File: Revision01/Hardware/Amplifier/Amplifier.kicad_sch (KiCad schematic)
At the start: 12 parts, among them U1 INA333AIDGKR, U2 TLV9061SQDBVRQ1

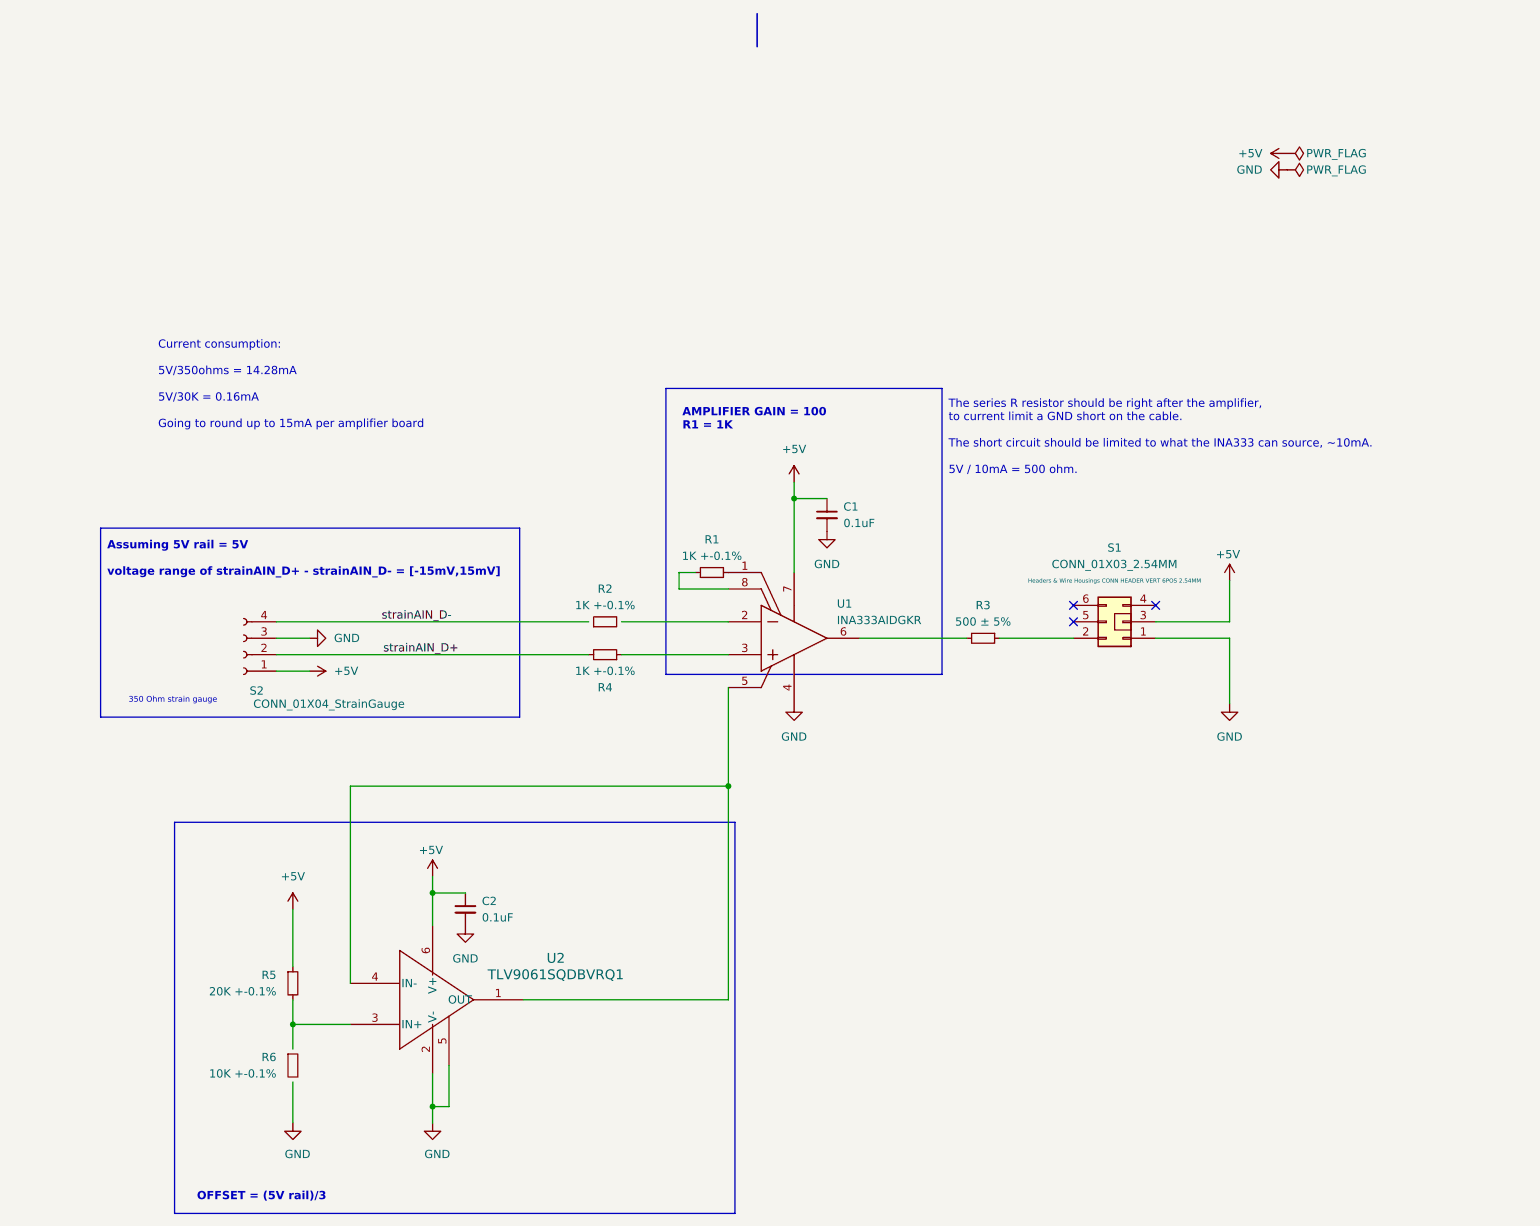
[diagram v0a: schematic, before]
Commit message: . Reverted Hardware/ changes to last known good commit f7a44a23fed9aca3ce7036a9f440c4d810a77518
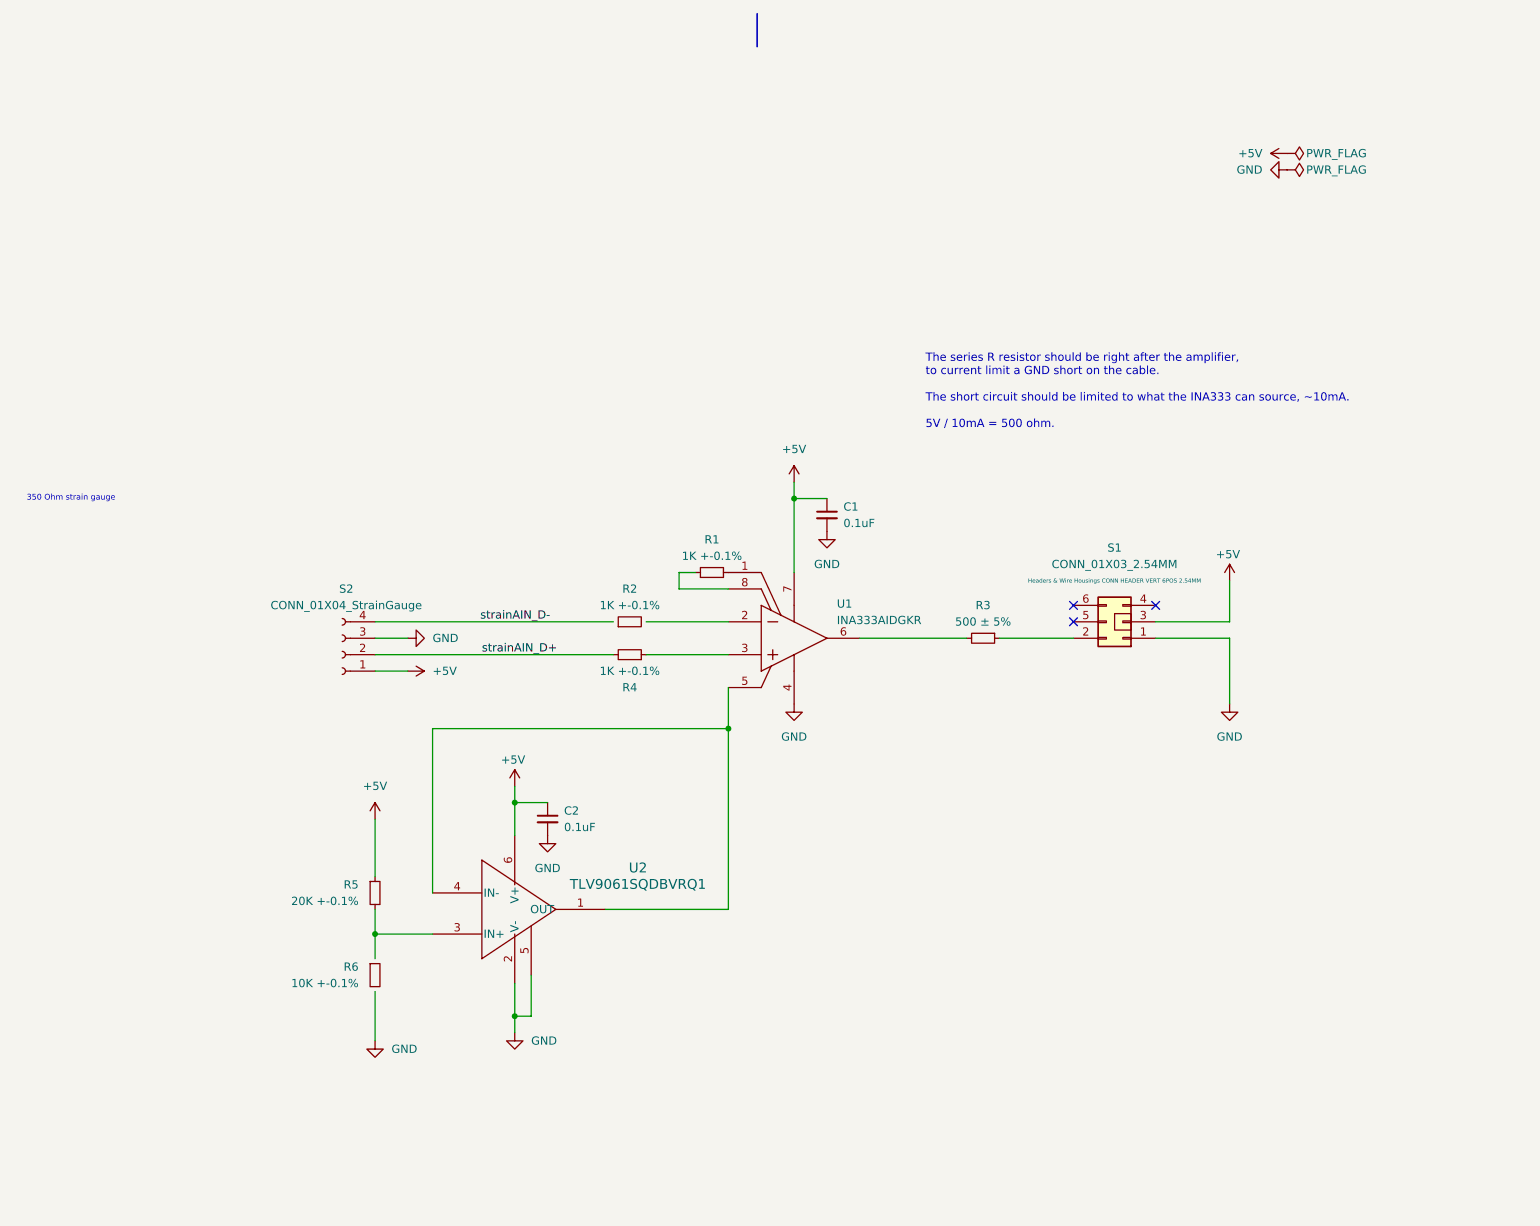
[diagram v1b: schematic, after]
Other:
- note removed: "AMPLIFIER GAIN = 100 R1 = 1K"
- note removed: "Assuming 5V rail = 5V voltage range of strainAIN_D+ - strainAIN_D- = [-15mV,15mV]"
- note removed: "Current consumption: 5V/350ohms = 14.28mA 5V/30K = 0.16mA Going to round up to 15mA per amplifier board"
- note removed: "OFFSET = (5V rail)/3"
- moved on the sheet: C2, R2, R4, R5, R6, S2, U2

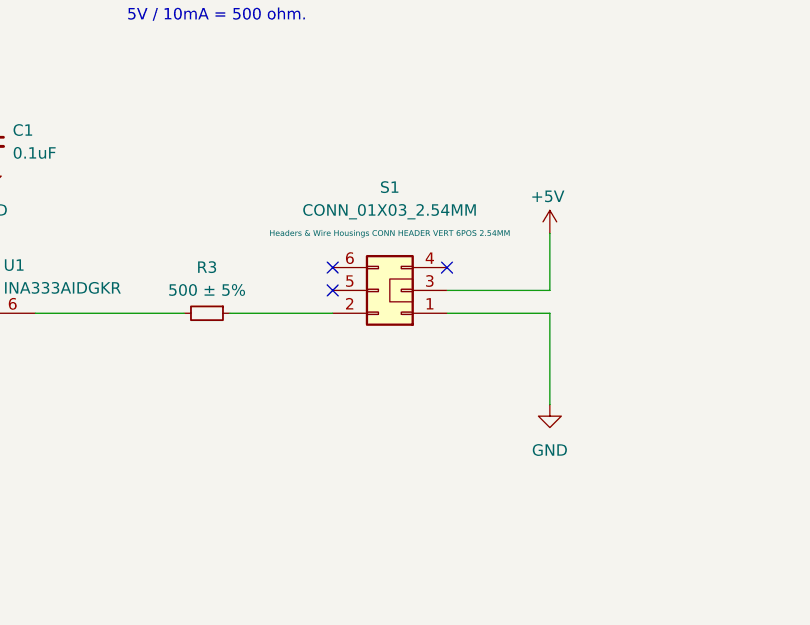
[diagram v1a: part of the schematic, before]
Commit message: . Hub & Amp: Changed wiring standard to GND SIG GND GND PWR GND . Hub: Added GND plane to 3.3V . Hub: Moved 1M pulldown resistor . Hub & Amp: Adjusted thermal relief tolerances . Hub: Changed buck convertor layout so capacitors are inline with feedback pin . Hub: Added stitching vias . Hub & Amp: Changed font sizes, changed silkscreen to be oriented one way
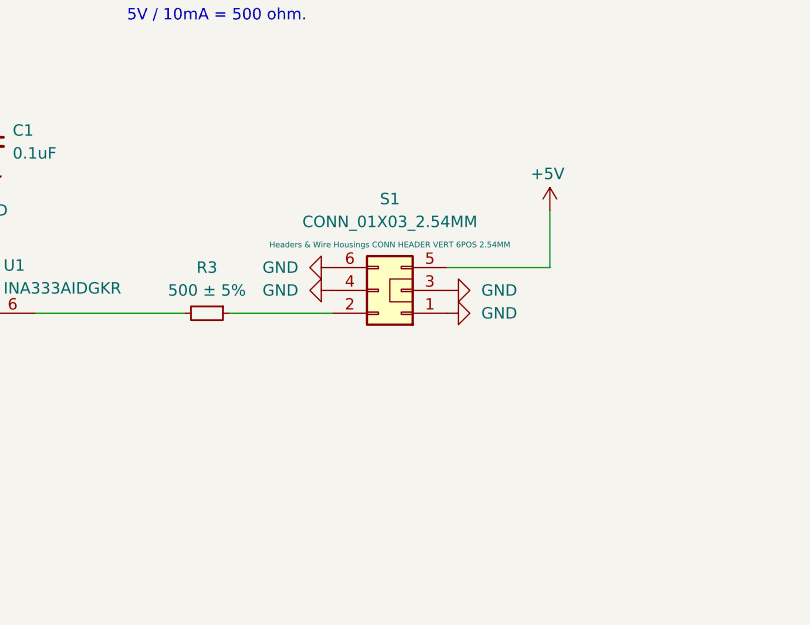
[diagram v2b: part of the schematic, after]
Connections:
- net +5V: now also S1.5 (Pin_5); no longer S1.3 (Pin_3)
- net GND: now also S1.3 (Pin_3), S1.4 (Pin_4), S1.6 (Pin_6)
- no-connect marks 3 -> 0
